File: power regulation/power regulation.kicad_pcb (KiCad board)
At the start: 4 copper layers, 175 x 100 mm, 95 parts, among them J1 Conn_01x02_Pin, J2 Conn_01x02_Pin, J3 Conn_01x02_Pin, M1 TO-236AB_SOT23_NEX, M2 TO-236AB_SOT23_NEX, U1 LT8640SEV_PBF, U2 LT8640SEV_PBF, U3 LT8619EDD-TRPBF

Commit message: Minor Traces changes
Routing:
- net DISPL_SCK: track 184.9 -> 184.3 mm
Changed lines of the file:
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@@
+	)
+	(segment
+		(start 99.5 108)
+		(end 99.5 98.32)
+		(width 0.2)
+		(layer "F.Cu")
+		(net 65)
 	)
 	(segment
@@
 	)
 	(segment
-		(start 151.4125 121.0875)
-		(end 135.5 137)
+		(start 134.5 137)
+		(end 94.4125 137)
 		(width 0.2)
 		(layer "F.Cu")
@@
 	)
 	(segment
+		(start 97 88.2)
+		(end 99 90.2)
+		(width 0.2)
+		(layer "F.Cu")
+		(net 65)
+	)
+	(segment
 		(start 151.4125 89)
-		(end 151.4125 121.0875)
+		(end 151.4125 120.0875)
 		(width 0.2)
 		(layer "F.Cu")
@@
 	)
 	(segment
-		(start 97 88.2)
-		(end 99 90.2)
+		(start 151.4125 120.0875)
+		(end 134.5 137)
+		(width 0.2)
+		(layer "F.Cu")
+		(net 65)
+	)
+	(segment
+		(start 99 94.5)
+		(end 97.68 95.82)
+		(width 0.2)
+		(layer "F.Cu")
+		(net 65)
+	)
+	(segment
+		(start 98 109.5)
+		(end 99.5 108)
 		(width 0.2)
 		(layer "F.Cu")
@@
 	)
 	(segment
+		(start 89.70625 132.29375)
+		(end 89.70625 115.79375)
+		(width 0.2)
+		(layer "F.Cu")
+		(net 65)
+	)
+	(segment
 		(start 94.4125 137)
 		(end 89.70625 132.29375)
-		(width 0.2)
-		(layer "F.Cu")
-		(net 65)
-	)
-	(segment
-		(start 99 94.5)
-		(end 97.68 95.82)
-		(width 0.2)
-		(layer "F.Cu")
-		(net 65)
-	)
-	(segment
-		(start 135.5 137)
-		(end 94.4125 137)
-		(width 0.2)
-		(layer "F.Cu")
-		(net 65)
-	)
-	(segment
-		(start 89.70625 132.29375)
-		(end 89.70625 115.79375)
-		(width 0.2)
-		(layer "F.Cu")
-		(net 65)
-	)
-	(segment
-		(start 99.5 108)
-		(end 99.5 98.32)
-		(width 0.2)
-		(layer "F.Cu")
-		(net 65)
-	)
-	(segment
-		(start 98 109.5)
-		(end 99.5 108)
 		(width 0.2)
 		(layer "F.Cu")
@@
 	)
 	(segment
-		(start 168.3625 73)
-		(end 204.4125 73)
-		(width 0.2)
-		(layer "B.Cu")
-		(net 71)
-	)
-	(segment
-		(start 166.4025 71.04)
-		(end 168.3625 73)
-		(width 0.2)
-		(layer "B.Cu")
-		(net 71)
-	)
-	(segment
 		(start 205.6625 71.75)
 		(end 205.6625 69)
@@
 	)
 	(segment
-		(start 204.4125 73)
+		(start 204.9125 72.5)
 		(end 205.6625 71.75)
+		(width 0.2)
+		(layer "B.Cu")
+		(net 71)
+	)
+	(segment
+		(start 166.4025 71.04)
+		(end 167.8625 72.5)
+		(width 0.2)
+		(layer "B.Cu")
+		(net 71)
+	)
+	(segment
+		(start 167.8625 72.5)
+		(end 204.9125 72.5)
 		(width 0.2)
 		(layer "B.Cu")
@@
 	)
 	(segment
-		(start 179.1625 110.11224)
-		(end 179.1625 110.25)
+		(start 196.25 113.25)
+		(end 205.6625 113.25)
 		(width 0.2)
 		(layer "B.Cu")
@@
 	)
 	(segment
-		(start 180.9125 112)
-		(end 192 112)
+		(start 178.5 109)
+		(end 180 110.5)
 		(width 0.2)
 		(layer "B.Cu")
@@
 	)
 	(segment
-		(start 192 112)
-		(end 193.25 113.25)
+		(start 173.02513 103.97487)
+		(end 178.05026 109)
 		(width 0.2)
 		(layer "B.Cu")
@@
 	)
 	(segment
-		(start 179.1625 110.25)
-		(end 180.9125 112)
+		(start 178.05026 109)
+		(end 178.5 109)
 		(width 0.2)
 		(layer "B.Cu")
@@
 	)
 	(segment
-		(start 173.02513 103.97487)
-		(end 179.1625 110.11224)
+		(start 180 110.5)
+		(end 193.5 110.5)
 		(width 0.2)
 		(layer "B.Cu")
@@
 	)
 	(segment
-		(start 193.25 113.25)
-		(end 205.6625 113.25)
+		(start 193.5 110.5)
+		(end 196.25 113.25)
 		(width 0.2)
 		(layer "B.Cu")
@@
 		(min_thickness 0.25)
 		(filled_areas_thickness no)
-		(fill yes
+		(fill
 			(thermal_gap 0.5)
 			(thermal_bridge_width 0.5)
@@
 		(min_thickness 0.25)
 		(filled_areas_thickness no)
-		(fill yes
+		(fill
 			(thermal_gap 0.5)
 			(thermal_bridge_width 0.5)
@@
 		(min_thickness 0.25)
 		(filled_areas_thickness no)
-		(fill yes
+		(fill
 			(thermal_gap 0.5)
 			(thermal_bridge_width 0.5)
@@
 		(min_thickness 0.25)
 		(filled_areas_thickness no)
-		(fill yes
+		(fill
 			(thermal_gap 0.5)
 			(thermal_bridge_width 0.5)
@@
 		(min_thickness 0.25)
 		(filled_areas_thickness no)
-		(fill yes
+		(fill
 			(thermal_gap 0.5)
 			(thermal_bridge_width 0.5)
@@
 		(min_thickness 0.25)
 		(filled_areas_thickness no)
-		(fill yes
+		(fill
 			(thermal_gap 0.5)
 			(thermal_bridge_width 0.5)
@@
 		(min_thickness 0.25)
 		(filled_areas_thickness no)
-		(fill yes
+		(fill
 			(thermal_gap 0.5)
 			(thermal_bridge_width 0.5)
@@
 		(min_thickness 0.25)
 		(filled_areas_thickness no)
-		(fill yes
+		(fill
 			(thermal_gap 0.5)
 			(thermal_bridge_width 0.5)
@@
 		(min_thickness 0.25)
 		(filled_areas_thickness no)
-		(fill yes
+		(fill
 			(thermal_gap 0.5)
 			(thermal_bridge_width 0.5)
@@
 		(min_thickness 0.25)
 		(filled_areas_thickness no)
-		(fill yes
+		(fill
 			(thermal_gap 0.5)
 			(thermal_bridge_width 0.5)
@@
 		(min_thickness 0.25)
 		(filled_areas_thickness no)
-		(fill yes
+		(fill
 			(thermal_gap 0.5)
 			(thermal_bridge_width 0.5)
@@
 		(min_thickness 0.25)
 		(filled_areas_thickness no)
-		(fill yes
+		(fill
 			(thermal_gap 0.5)
 			(thermal_bridge_width 0.5)
@@
 		(min_thickness 0.25)
 		(filled_areas_thickness no)
-		(fill yes
+		(fill
 			(thermal_gap 0.5)
 			(thermal_bridge_width 0.5)
@@
 		(min_thickness 0.25)
 		(filled_areas_thickness no)
-		(fill yes
+		(fill
 			(thermal_gap 0.5)
 			(thermal_bridge_width 0.5)
@@
 		(min_thickness 0.25)
 		(filled_areas_thickness no)
-		(fill yes
+		(fill
 			(thermal_gap 0.5)
 			(thermal_bridge_width 0.5)
@@
 		(min_thickness 0.25)
 		(filled_areas_thickness no)
-		(fill yes
+		(fill
 			(thermal_gap 0.5)
 			(thermal_bridge_width 0.5)
@@
 		(min_thickness 0.25)
 		(filled_areas_thickness no)
-		(fill yes
+		(fill
 			(thermal_gap 0.5)
 			(thermal_bridge_width 0.5)
@@
 		(min_thickness 0.25)
 		(filled_areas_thickness no)
-		(fill yes
+		(fill
 			(thermal_gap 0.5)
 			(thermal_bridge_width 0.5)
@@
 		(min_thickness 0.25)
 		(filled_areas_thickness no)
-		(fill yes
+		(fill
 			(thermal_gap 0.5)
 			(thermal_bridge_width 0.5)
@@
 		(min_thickness 0.25)
 		(filled_areas_thickness no)
-		(fill yes
+		(fill
 			(thermal_gap 0.5)
 			(thermal_bridge_width 0.5)
@@
 		(min_thickness 0.25)
 		(filled_areas_thickness no)
-		(fill yes
+		(fill
 			(thermal_gap 0.5)
 			(thermal_bridge_width 0.5)
@@
 		(min_thickness 0.25)
 		(filled_areas_thickness no)
-		(fill yes
+		(fill
 			(thermal_gap 0.5)
 			(thermal_bridge_width 0.5)
@@
 		(min_thickness 0.25)
 		(filled_areas_thickness no)
-		(fill yes
+		(fill
 			(thermal_gap 0.5)
 			(thermal_bridge_width 0.5)
@@
 		(min_thickness 0.25)
 		(filled_areas_thickness no)
-		(fill yes
+		(fill
 			(thermal_gap 0.5)
 			(thermal_bridge_width 0.5)

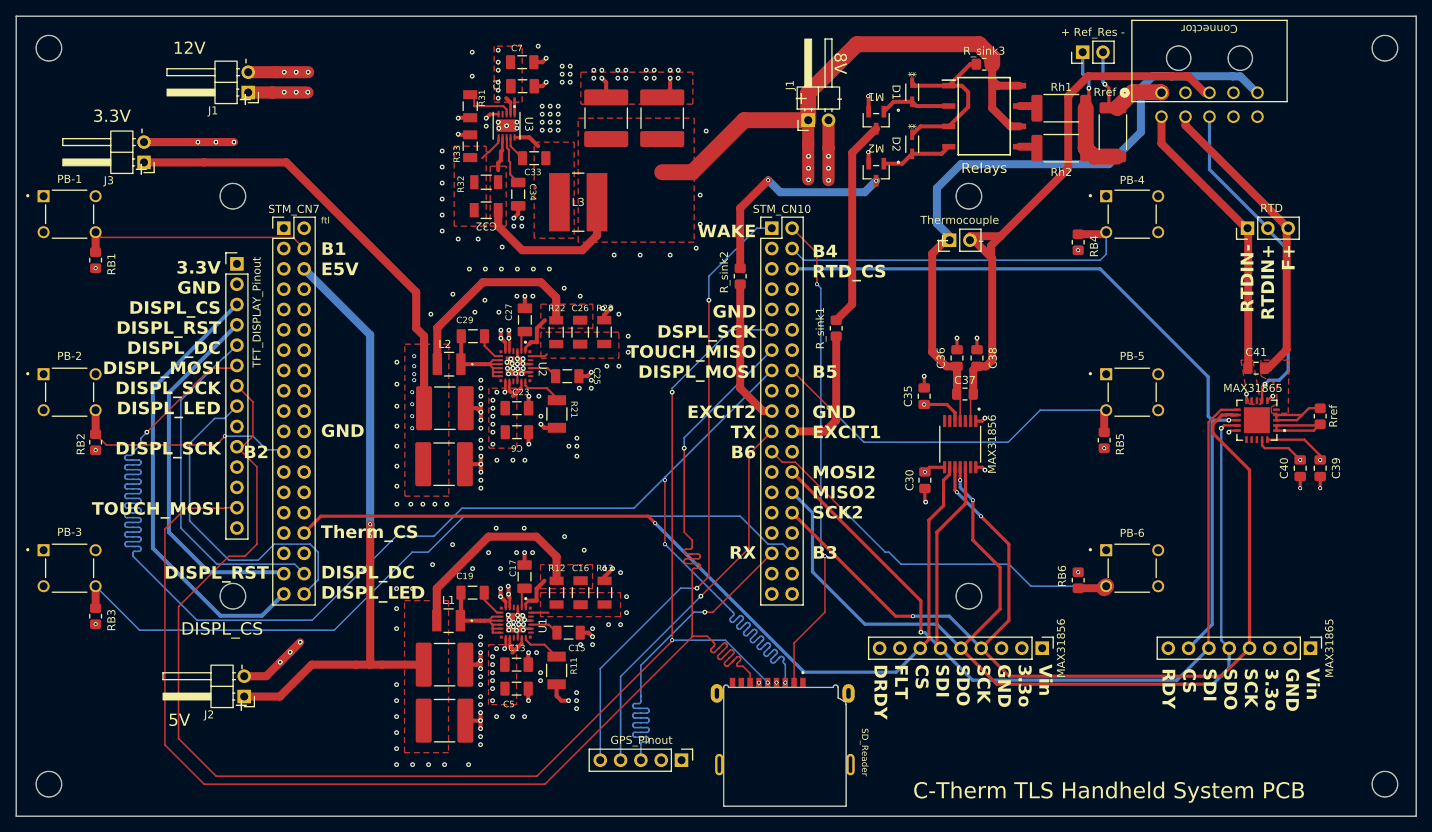
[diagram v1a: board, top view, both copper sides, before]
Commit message: Create designator for relay and max ICs.
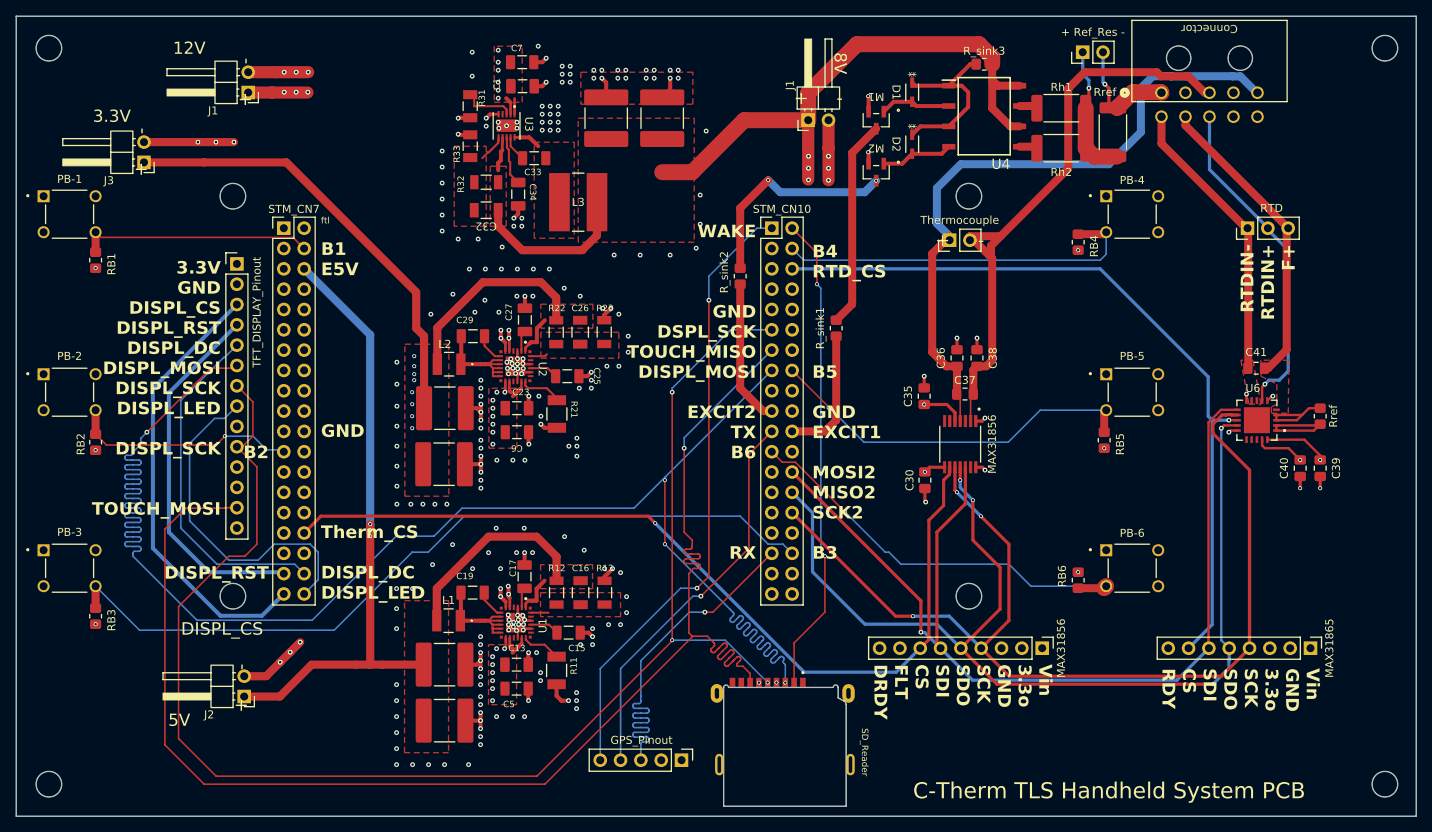
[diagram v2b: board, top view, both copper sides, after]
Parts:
- renumbered Relays to U4, MAX31865 to U6
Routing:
- net Thermocouple-: track 73.8 -> 74.8 mm
- net TX: track 48.9 -> 49.5 mm

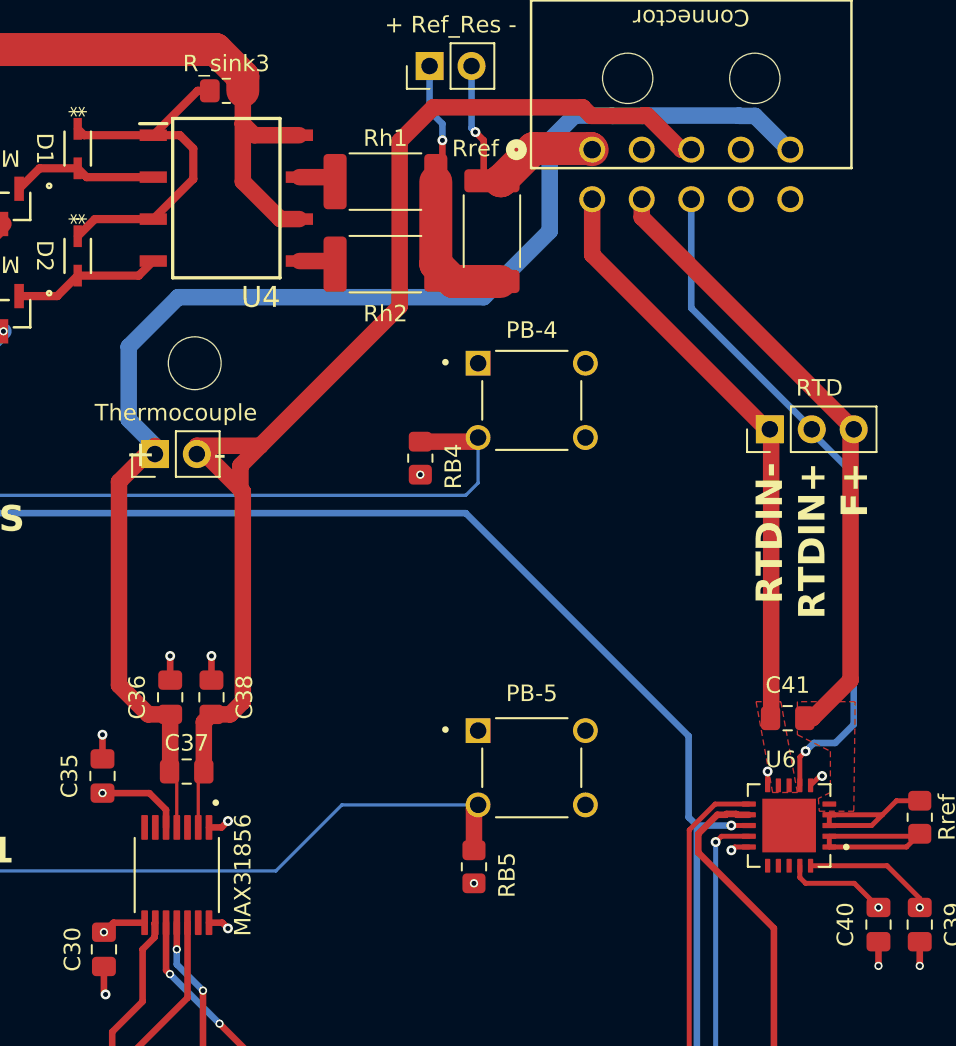
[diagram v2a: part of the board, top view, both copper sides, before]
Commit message: Fix Wiring of thermocouple module and trace widths
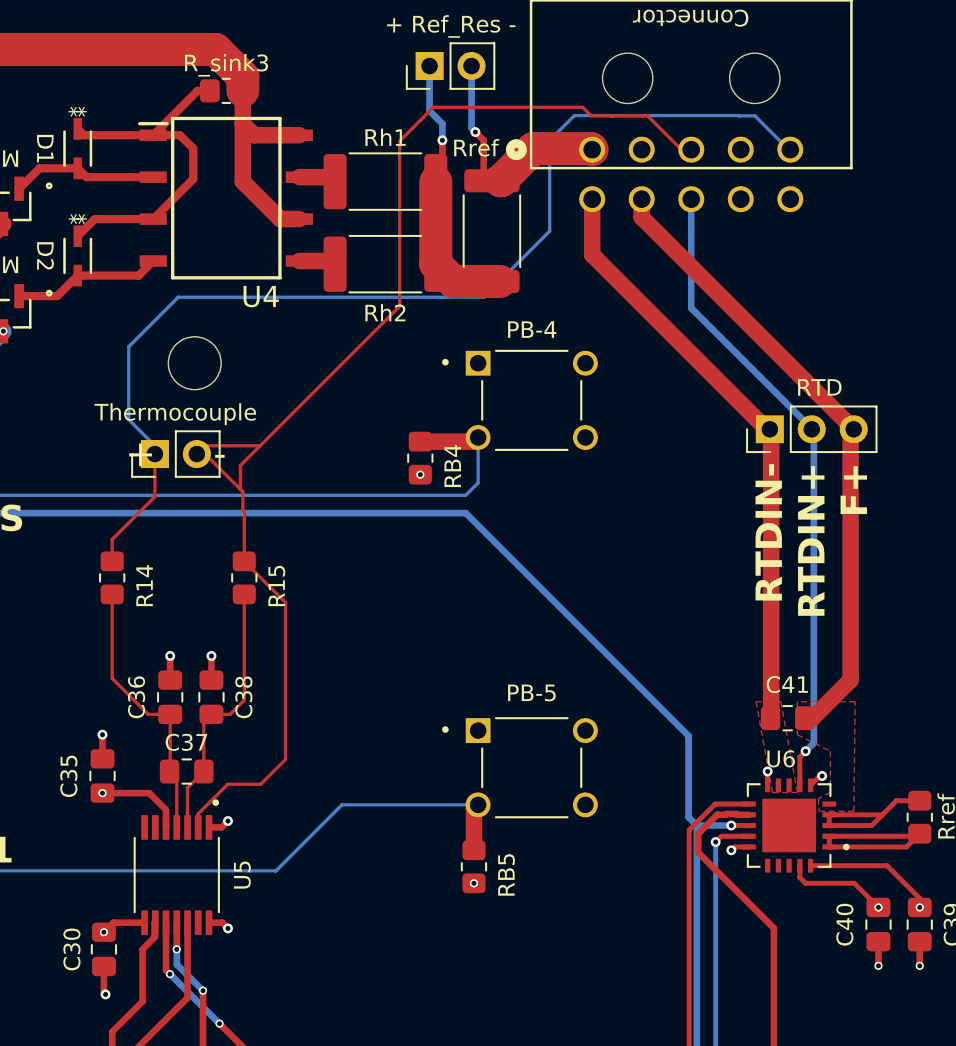
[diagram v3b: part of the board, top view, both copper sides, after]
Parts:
- added R14: R_0805_2012Metric_Pad1.20x1.40mm_HandSolder, Resistor_SMD:R_0805_2012Metric_Pad1.20x1.40mm_HandSolder, F.Cu at (183.5, 77.5)
- added R15: R_0805_2012Metric_Pad1.20x1.40mm_HandSolder, Resistor_SMD:R_0805_2012Metric_Pad1.20x1.40mm_HandSolder, F.Cu at (191.5, 77.5)
- renumbered MAX31856 to U5
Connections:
- C36 pad 2: Thermocouple+ -> Thermocouple++
- C37 pad 1: Thermocouple- -> Thermocouple--
- C37 pad 2: Thermocouple+ -> Thermocouple++
- C38 pad 1: Thermocouple- -> Thermocouple--
- U5 pad 3: Thermocouple- -> Thermocouple--
- U5 pad 4: Thermocouple+ -> Thermocouple++
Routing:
- net Thermocouple+: track 82.9 -> 64.7 mm
- net Thermocouple++: track 0.00 -> 16.5 mm
- net Thermocouple--: track 0.00 -> 16.2 mm
- net RTDSens: track 41.7 -> 38.9 mm
- net Thermocouple-: track 74.8 -> 77.4 mm

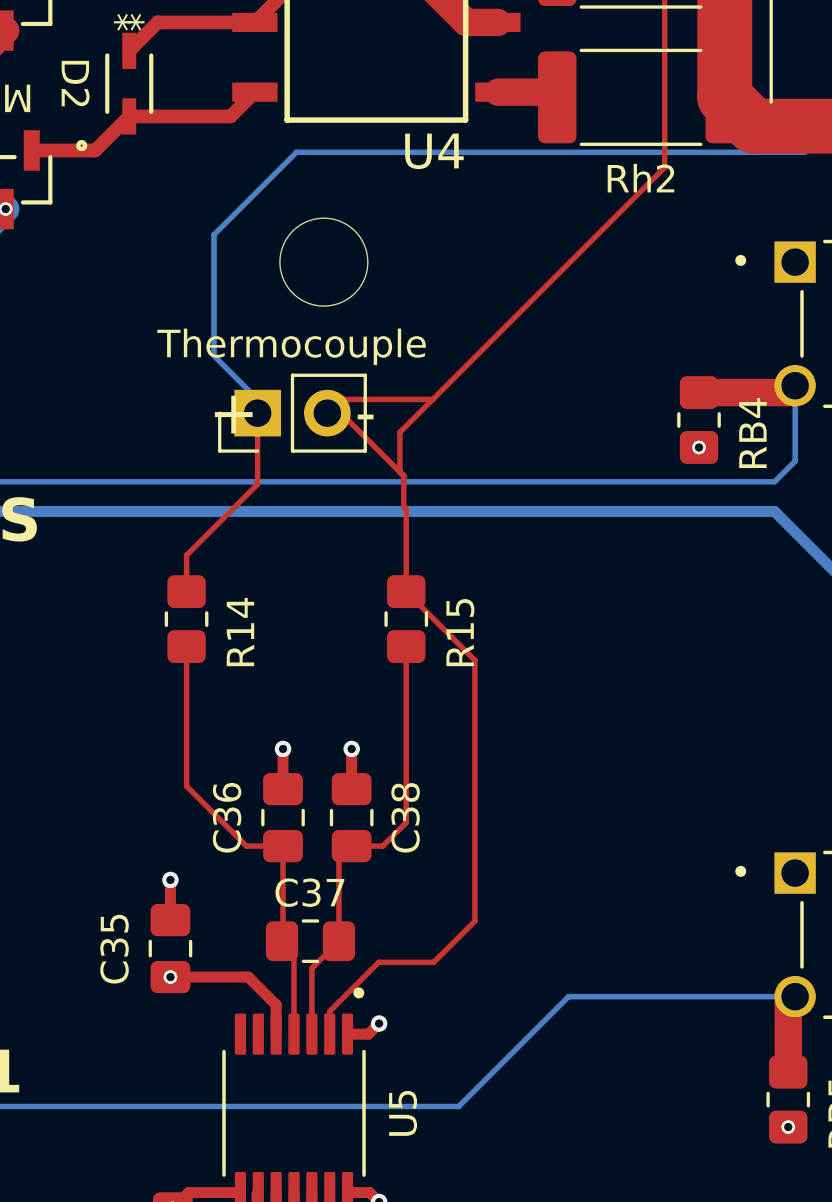
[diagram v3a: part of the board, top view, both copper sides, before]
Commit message: Remove thermocouple resistors. Not need only good for overvoltage protection above 40 V.
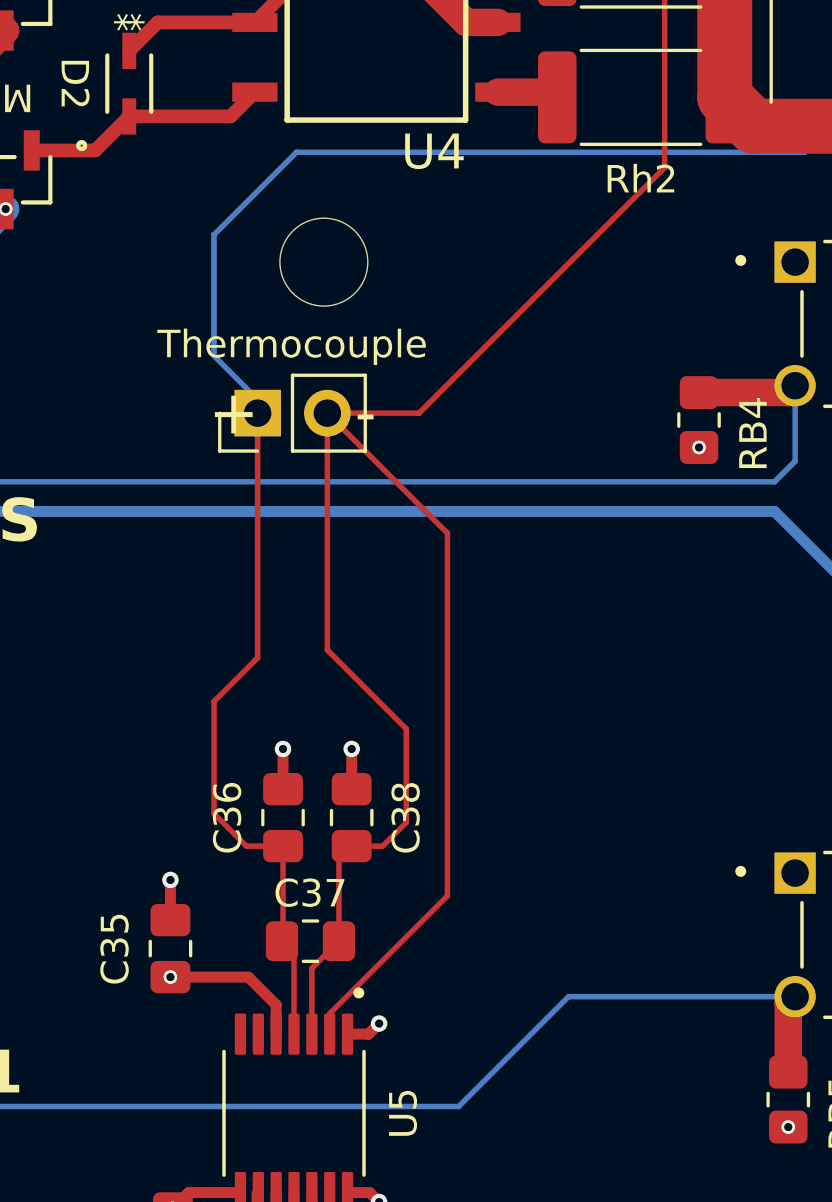
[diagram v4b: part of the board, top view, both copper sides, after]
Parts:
- removed R14, R15: R_0805_2012Metric_Pad1.20x1.40mm_HandSolder, Resistor_SMD:R_0805_2012Metric_Pad1.20x1.40mm_HandSolder
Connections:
- C37 pad 1: Thermocouple-- -> Thermocouple-
- C37 pad 2: Thermocouple++ -> Thermocouple+
- C38 pad 1: Thermocouple-- -> Thermocouple-
- U5 pad 3: Thermocouple-- -> Thermocouple-
- U5 pad 4: Thermocouple++ -> Thermocouple+
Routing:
- net Thermocouple-: track 77.4 -> 98.9 mm
- net Thermocouple+: track 64.7 -> 82.4 mm
- net Thermocouple++: track 16.5 -> 0.00 mm
- net Thermocouple--: track 16.2 -> 0.00 mm
